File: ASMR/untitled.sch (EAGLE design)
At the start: 57 parts, among them J3 2172034-1, J4 POWER_JACKSLT, Q1 MMBT3904, Q2 MMBT3904, Q3 12MHz, Q4 MC-406, U2 DS1307Z+, U3 MAX3444EASA, U4 AMS1117, U5 MAX232CSE

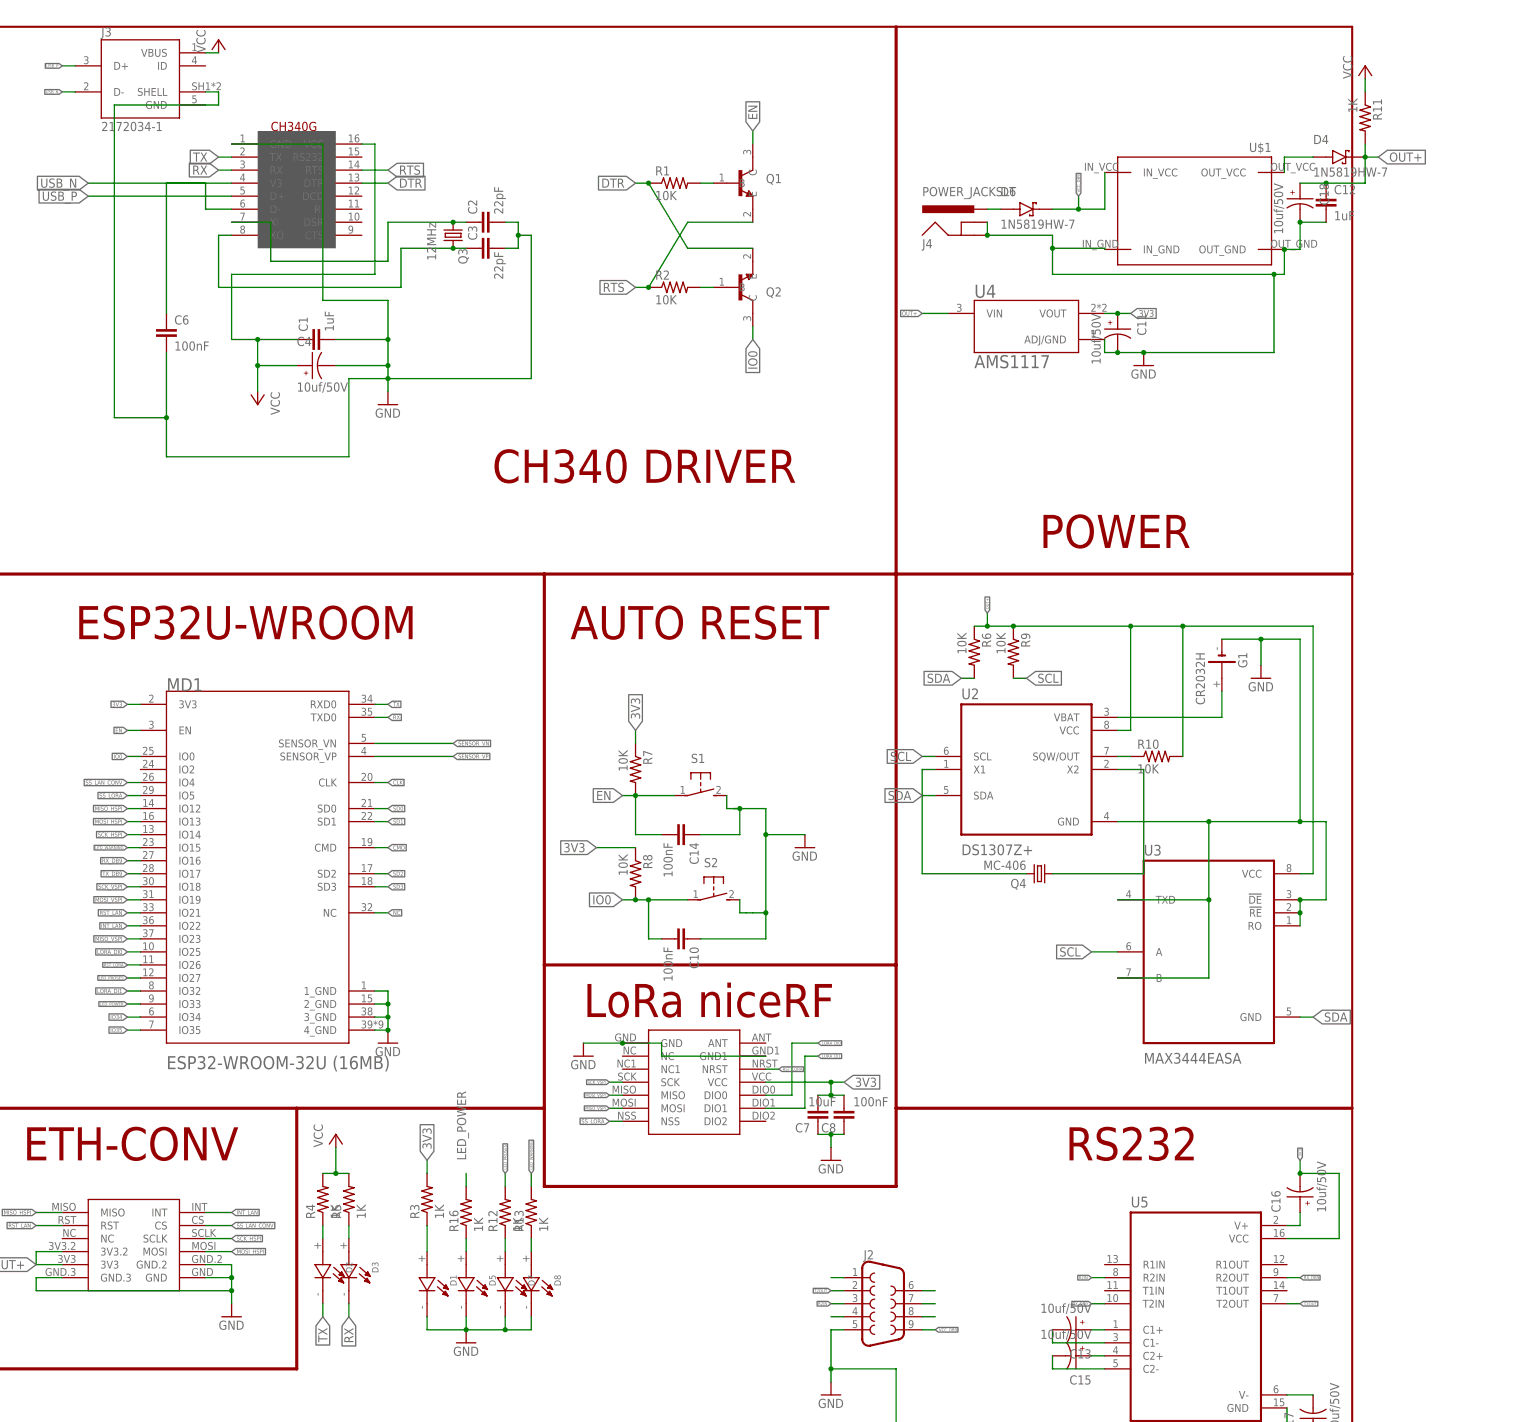
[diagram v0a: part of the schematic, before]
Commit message: revisi .sch dan membuat.brd
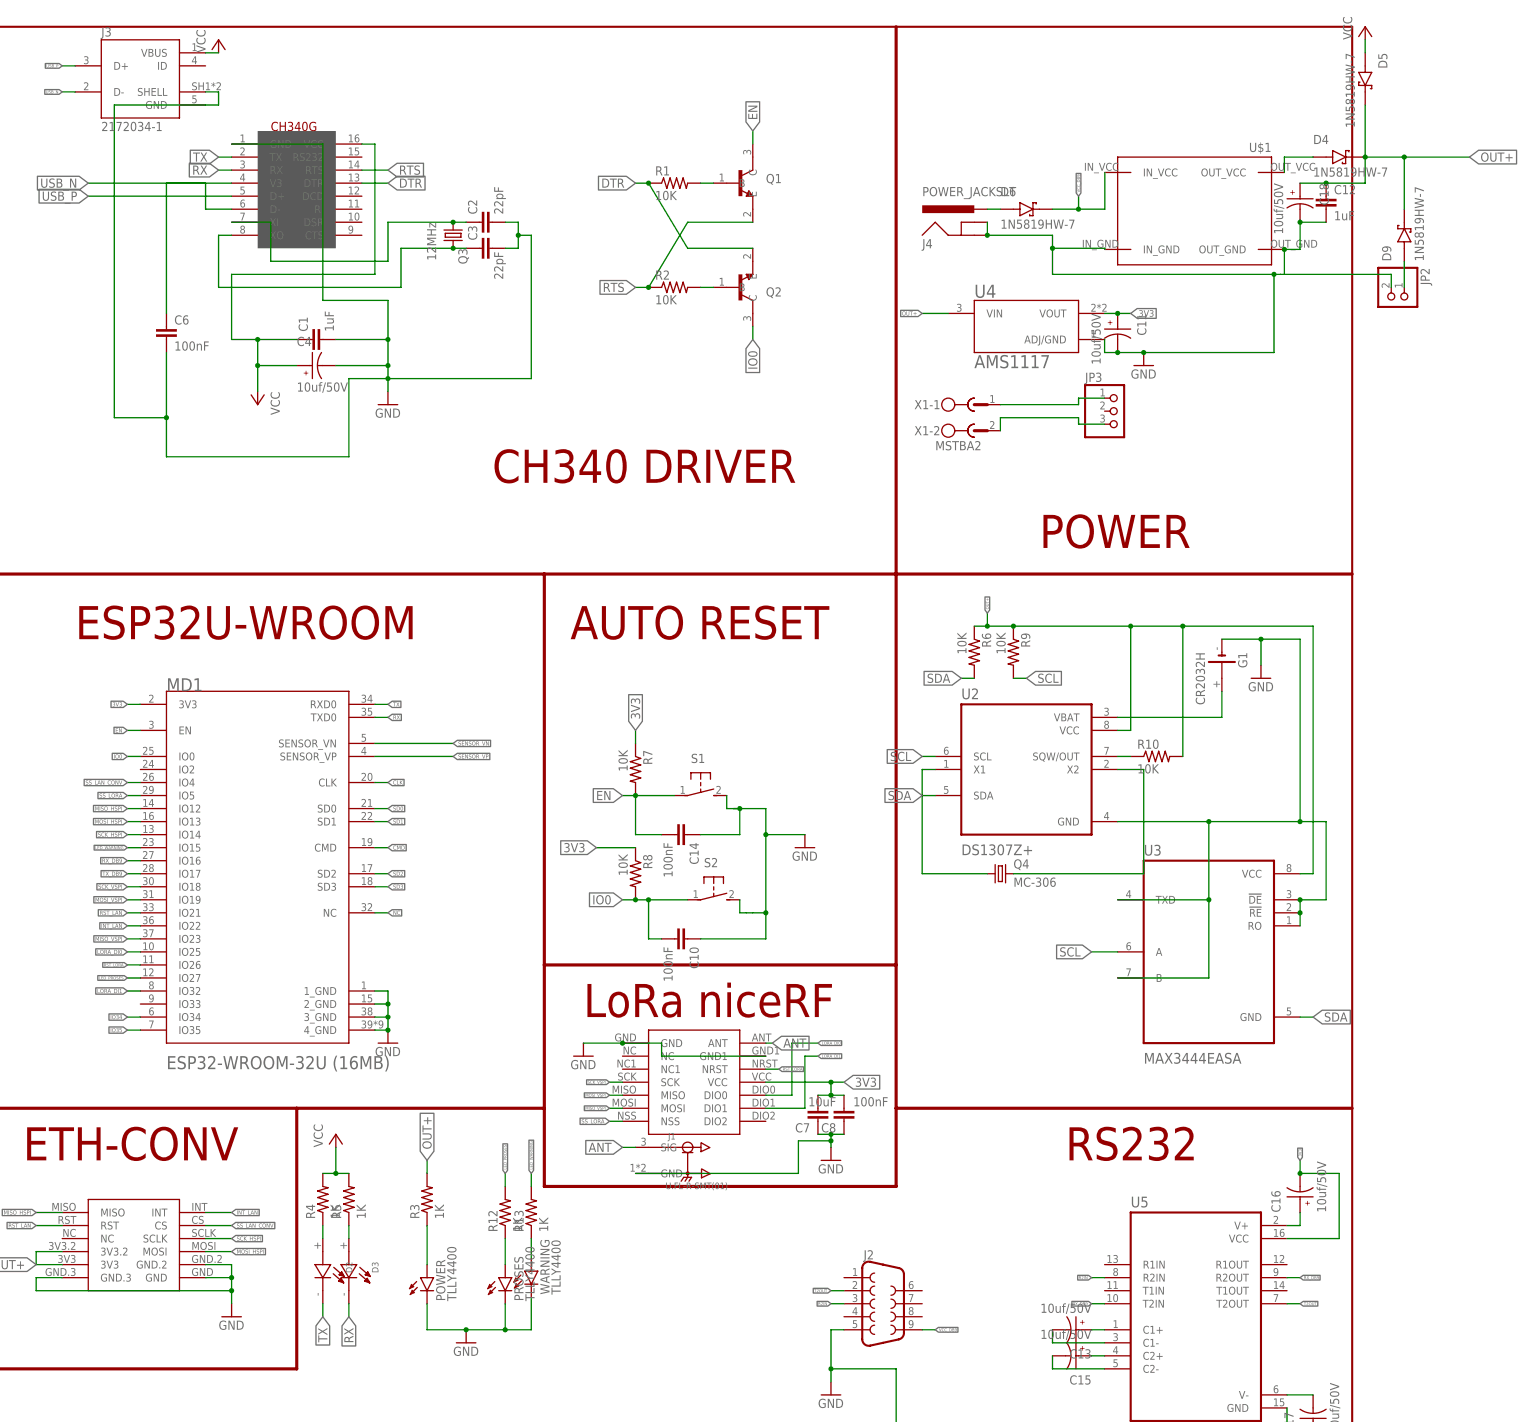
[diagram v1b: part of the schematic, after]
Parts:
- removed D1: 3v3, LHN974_RED_LED_1206:LHN974_RED_LED_1206
- removed D7, D8: 3v31, LHN974_RED_LED_1206:LHN974_RED_LED_1206
- removed R11, R16: 1K, adafruit:R-US_M0805
- added D9: 1N5819HW-7, 1N5819HW-7:1N5819HW-7
- added J1: U.FL-R-SMT(01), U.FL-R-SMT_01_:U.FL-R-SMT(01)
- added JP2: (no value), pinhead:PINHD-1X2
- added JP3: (no value), pinhead:PINHD-1X3
- added POWER, PROSES, WARNING: TLLY4400, led:TLLY4400
- added X1: MSTBA2, con-phoenix-508:MSTBA2
- D5: value 3v31 -> 1N5819HW-7; device LHN974_RED_LED_1206:LHN974_RED_LED_1206 -> 1N5819HW-7:1N5819HW-7
- Q4: value MC-406 -> MC-306; device crystal:MC-406 -> crystal:MC-306
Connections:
- removed net LED_POWER: MD1.IO33, R16.2
- removed net N$20: J2.6
- removed net N$21: J2.7
- removed net N$22: J2.8
- new net ANT: J1.SIG, LORA-NICERF-V1.ANT
- net 3V3: no longer R3.2
- net GND: now also J1.GND, JP2.2, POWER.C, PROSES.C, WARNING.C; no longer D1.-, D5.-, D7.-, D8.-
- net N$13: now also JP3.1, X1-1.1; no longer J2.1
- net N$16: now also JP3.3, X1-2.1; no longer D5.+, R16.1
- net N$17: now also D9.A, JP2.1; no longer J2.4
- net N$25: now also PROSES.A; no longer D7.+
- net N$28: now also WARNING.A; no longer D8.+
- net N$3: now also POWER.A; no longer D1.+
- net N$6: now also Q4.1; no longer Q4.2
- net N$7: now also Q4.2; no longer Q4.1
- net OUT+: now also D5.K, D9.K, R3.2; no longer R11.2
- net VCC: now also D5.A; no longer R11.1
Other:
- moved on the sheet: Q4

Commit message: penambahan komponen
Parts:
- added D1: 1N5819HW-7, 1N5819HW-7:1N5819HW-7
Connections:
- new net N$20: D1.A, J2.9
- net OUT+: now also D1.K
- net VCC_DB9: no longer J2.9
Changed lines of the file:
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@@
 <part name="J1" library="U.FL-R-SMT_01_" deviceset="U.FL-R-SMT(01)" device=""/>
 <part name="JP3" library="pinhead" library_urn="urn:adsk.eagle:library:325" deviceset="PINHD-1X3" device="" package3d_urn="urn:adsk.eagle:package:22458/2"/>
+<part name="D1" library="1N5819HW-7" deviceset="1N5819HW-7" device=""/>
 </parts>
 <sheets>
@@
 <attribute name="NAME" x="85.09" y="121.285" size="1.778" layer="95"/>
 <attribute name="VALUE" x="85.09" y="107.95" size="1.778" layer="96"/>
+</instance>
+<instance part="D1" gate="G$1" x="59.69" y="-63.5" smashed="yes">
+<attribute name="NAME" x="54.61" y="-60.96" size="1.778" layer="95"/>
+<attribute name="VALUE" x="54.61" y="-67.31" size="1.778" layer="96"/>
 </instance>
 </instances>
@@
 <label x="-43.18" y="-30.48" size="1.778" layer="95" rot="R90" xref="yes"/>
 </segment>
+<segment>
+<pinref part="D1" gate="G$1" pin="K"/>
+<wire x1="64.77" y1="-63.5" x2="66.04" y2="-63.5" width="0.1524" layer="91"/>
+<label x="66.04" y="-64.77" size="1.778" layer="95"/>
+</segment>
 </net>
 <net name="MISO_HSPI" class="0">
@@
 </net>
 <net name="VCC_DB9" class="0">
-<segment>
-<pinref part="J2" gate="G$1" pin="9"/>
-<wire x1="53.34" y1="-63.5" x2="55.88" y2="-63.5" width="0.1524" layer="91"/>
-<label x="55.88" y="-63.5" size="0.6096" layer="95" xref="yes"/>
-</segment>
 <segment>
 <pinref part="D6" gate="G$1" pin="K"/>
@@
 </segment>
 </net>
+<net name="N$20" class="0">
+<segment>
+<pinref part="J2" gate="G$1" pin="9"/>
+<pinref part="D1" gate="G$1" pin="A"/>
+<wire x1="53.34" y1="-63.5" x2="54.61" y2="-63.5" width="0.1524" layer="91"/>
+</segment>
+</net>
